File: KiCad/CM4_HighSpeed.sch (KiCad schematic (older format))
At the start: 12 parts, among them J1 Conn_02x02_Odd_Even, J2 Conn_01x22_Female, J3 Conn_01x22_Female, J4 Conn_01x22_Female, J5 Conn_01x22_Female, J6 1888811-1, U5 AP2822CKETR-G1

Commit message: Removing Display0 and Camera0
Eliminates the need for J1, R1 and R2. Also removed.
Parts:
- removed J1: Conn_02x02_Odd_Even, CM4_MATX:PinHeader_2x02_P2.54mm_Vertical, symbol Connector_Generic:Conn_02x02_Odd_Even
- removed J2, J4: Conn_01x22_Female, CM4_MATX:Hirose_FH12-22S-0.5SH_1x22-1MP_P0.50mm_Horizontal, symbol Connector:Conn_01x22_Female
- removed R1, R2: 2.2K 1%, symbol Device:R_Small
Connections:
- net labels removed: GPIO_VREF, ID_SC, ID_SD, SCL1, SDA1
- wire segments 299 -> 241
- no-connect marks 19 -> 8
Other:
- note added: "Camera Connector"
- note added: "Display Connector"
- note removed: "Camera Connectors"
- note removed: "Display Connectors"
- note removed: "Jumpers to be fitted if Camera0 or Display0 are used"
- moved on the sheet: J3, J5

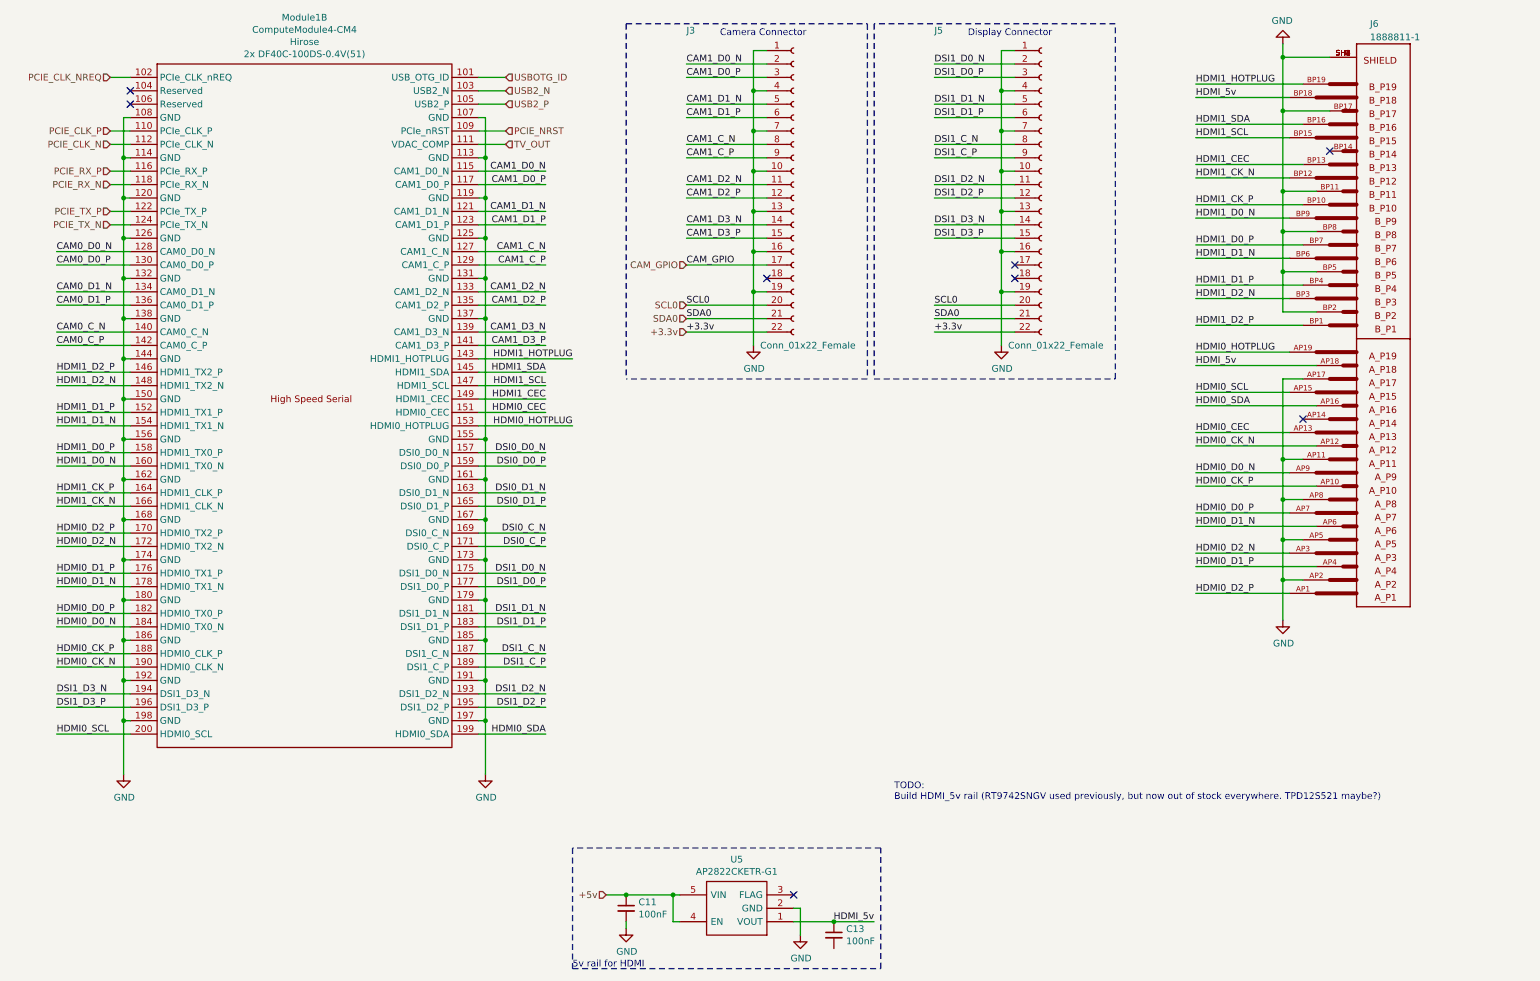
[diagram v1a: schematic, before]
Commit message: PCIe Wiring, resistor value adjustments, and a bunch of small ERC fixes.
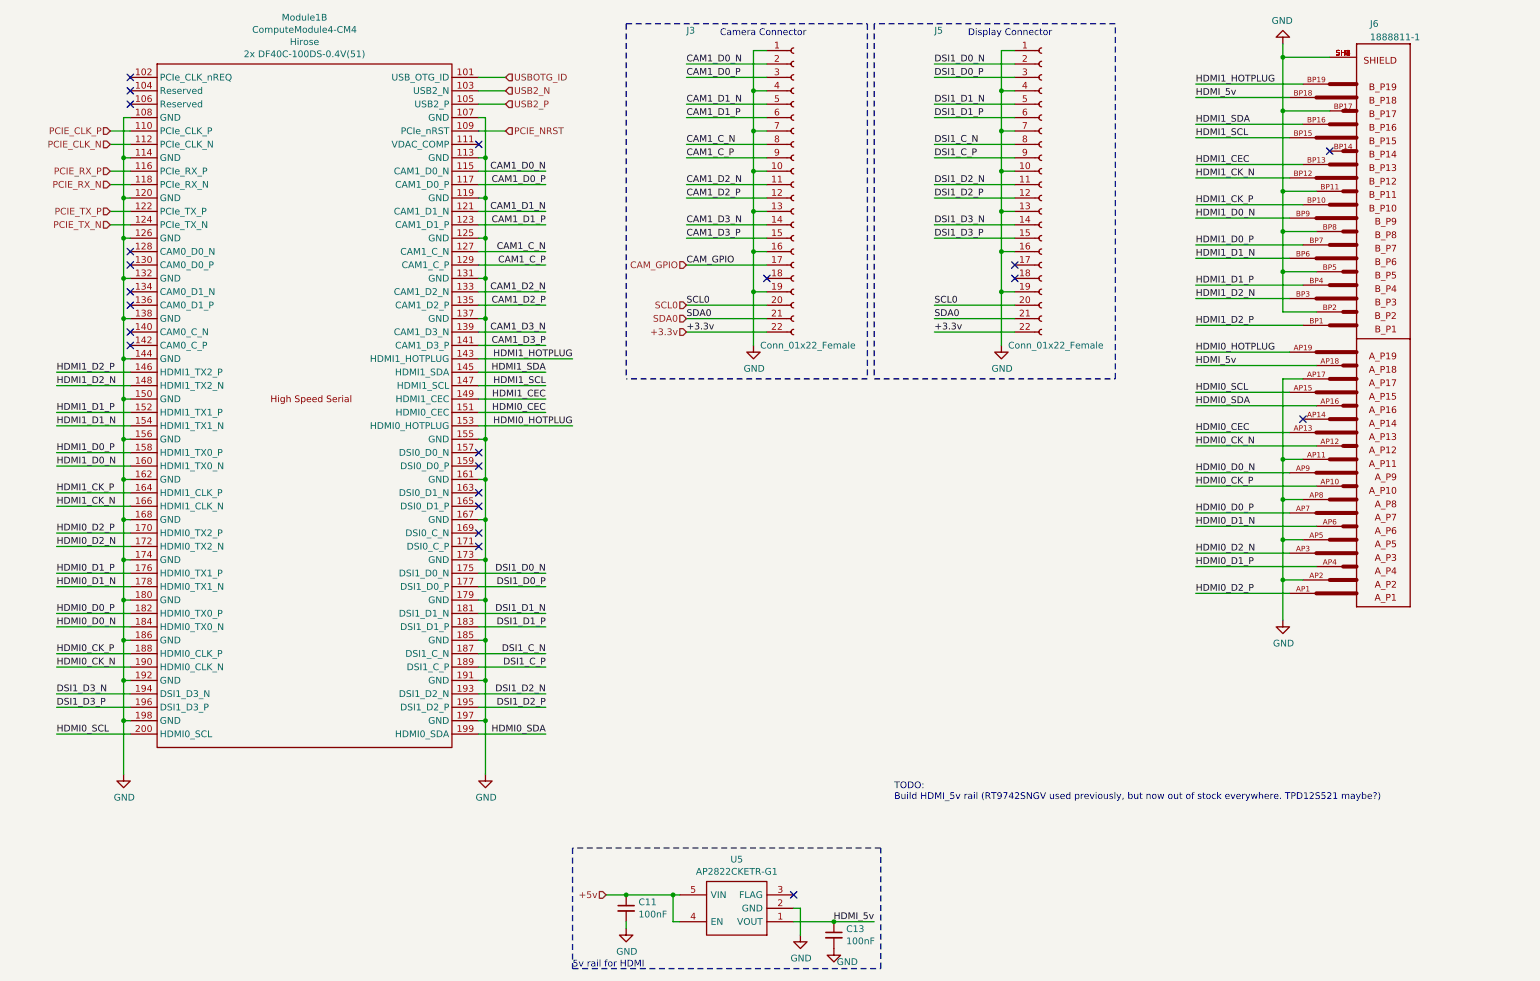
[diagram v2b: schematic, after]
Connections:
- net GND: now also C13.2
- net CAM0_C_N: no longer names the net of Module1.140 (CAM0_C_N)
- net CAM0_C_P: no longer names the net of Module1.142 (CAM0_C_P)
- net CAM0_D0_N: no longer names the net of Module1.128 (CAM0_D0_N)
- net CAM0_D0_P: no longer names the net of Module1.130 (CAM0_D0_P)
- net CAM0_D1_N: no longer names the net of Module1.134 (CAM0_D1_N)
- net CAM0_D1_P: no longer names the net of Module1.136 (CAM0_D1_P)
- net DSI0_C_N: no longer names the net of Module1.169 (DSI0_C_N)
- net DSI0_C_P: no longer names the net of Module1.171 (DSI0_C_P)
- net DSI0_D0_N: no longer names the net of Module1.157 (DSI0_D0_N)
- net DSI0_D0_P: no longer names the net of Module1.159 (DSI0_D0_P)
- net DSI0_D1_N: no longer names the net of Module1.163 (DSI0_D1_N)
- net DSI0_D1_P: no longer names the net of Module1.165 (DSI0_D1_P)
- net PCIE_CLK_NREQ: no longer names the net of Module1.102 (PCIe_CLK_nREQ)
- net TV_OUT: no longer names the net of Module1.111 (VDAC_COMP)
- no-connect marks 8 -> 22
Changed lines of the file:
@@
 Wire Wire Line
 	3950 1700 3950 2000
-Wire Wire Line
-	1150 1100 1300 1100
 $Comp
 L CM4_MATX:ComputeModule4-CM4 Module1
@@
 NoConn ~ 1300 1200
 NoConn ~ 1300 1300
-Text Label 750  2400 0    50   ~ 0
-CAM0_D0_N
-Text Label 750  2500 0    50   ~ 0
-CAM0_D0_P
-Text Label 750  2700 0    50   ~ 0
-CAM0_D1_N
-Text Label 750  2800 0    50   ~ 0
-CAM0_D1_P
-Text Label 750  3000 0    50   ~ 0
-CAM0_C_N
-Text Label 750  3100 0    50   ~ 0
-CAM0_C_P
 Text Label 750  3300 0    50   ~ 0
 HDMI1_D2_P
@@
 Text Label 4400 5400 2    50   ~ 0
 DSI1_C_N
-Text Label 4400 4600 2    50   ~ 0
-DSI0_C_P
-Text Label 4400 4500 2    50   ~ 0
-DSI0_C_N
-Text Label 4400 4300 2    50   ~ 0
-DSI0_D1_P
-Text Label 4400 4200 2    50   ~ 0
-DSI0_D1_N
-Text Label 4400 4000 2    50   ~ 0
-DSI0_D0_P
-Text Label 4400 3900 2    50   ~ 0
-DSI0_D0_N
 Text Label 4400 3600 2    50   ~ 0
 HDMI0_CEC
@@
 Text Label 4400 1800 2    50   ~ 0
 CAM1_D0_N
-Text HLabel 4100 1600 2    50   Input ~ 0
-TV_OUT
 Text HLabel 4100 1500 2    50   Input ~ 0
 PCIE_NRST
@@
 	3900 1500 4100 1500
 Wire Wire Line
-	3900 1600 4100 1600
-Wire Wire Line
 	3900 1800 4400 1800
 Wire Wire Line
@@
 Wire Wire Line
 	4600 3700 3900 3700
-Wire Wire Line
-	4400 3900 3900 3900
-Wire Wire Line
-	3900 4000 4400 4000
-Wire Wire Line
-	4400 4200 3900 4200
-Wire Wire Line
-	3900 4300 4400 4300
-Wire Wire Line
-	4400 4500 3900 4500
-Wire Wire Line
-	3900 4600 4400 4600
 Wire Wire Line
 	4400 4800 3900 4800
@@
 Wire Wire Line
 	750  3300 1300 3300
-Wire Wire Line
-	1300 3100 750  3100
-Wire Wire Line
-	750  3000 1300 3000
-Wire Wire Line
-	1300 2800 750  2800
-Wire Wire Line
-	750  2700 1300 2700
-Wire Wire Line
-	1300 2500 750  2500
-Wire Wire Line
-	1300 2400 750  2400
 Wire Wire Line
 	1300 2200 1150 2200
@@
 Text HLabel 5450 2500 0    50   Input ~ 0
 CAM_GPIO
-Text HLabel 1150 1100 0    50   Input ~ 0
-PCIE_CLK_NREQ
 Text HLabel 1150 1500 0    50   Input ~ 0
 PCIE_CLK_P
@@
 Wire Notes Line
 	8650 700  6850 700
+NoConn ~ 3900 1600
+NoConn ~ 1300 3100
+NoConn ~ 1300 3000
+NoConn ~ 1300 2800
+NoConn ~ 1300 2700
+NoConn ~ 1300 2500
+NoConn ~ 1300 2400
+NoConn ~ 1300 1100
+$Comp
+L power:GND #PWR0232
+U 1 1 6024C813
+P 6550 7600
+F 0 "#PWR0232" H 6550 7350 50  0001 C CNN
+F 1 "GND" H 6650 7500 50  0000 C CNN
+F 2 "" H 6550 7600 50  0001 C CNN
+F 3 "" H 6550 7600 50  0001 C CNN
+	1    6550 7600
+	1    0    0    -1
+$EndComp
+NoConn ~ 3900 4600
+NoConn ~ 3900 4500
+NoConn ~ 3900 4300
+NoConn ~ 3900 4200
+NoConn ~ 3900 4000
+NoConn ~ 3900 3900
 $EndSCHEMATC

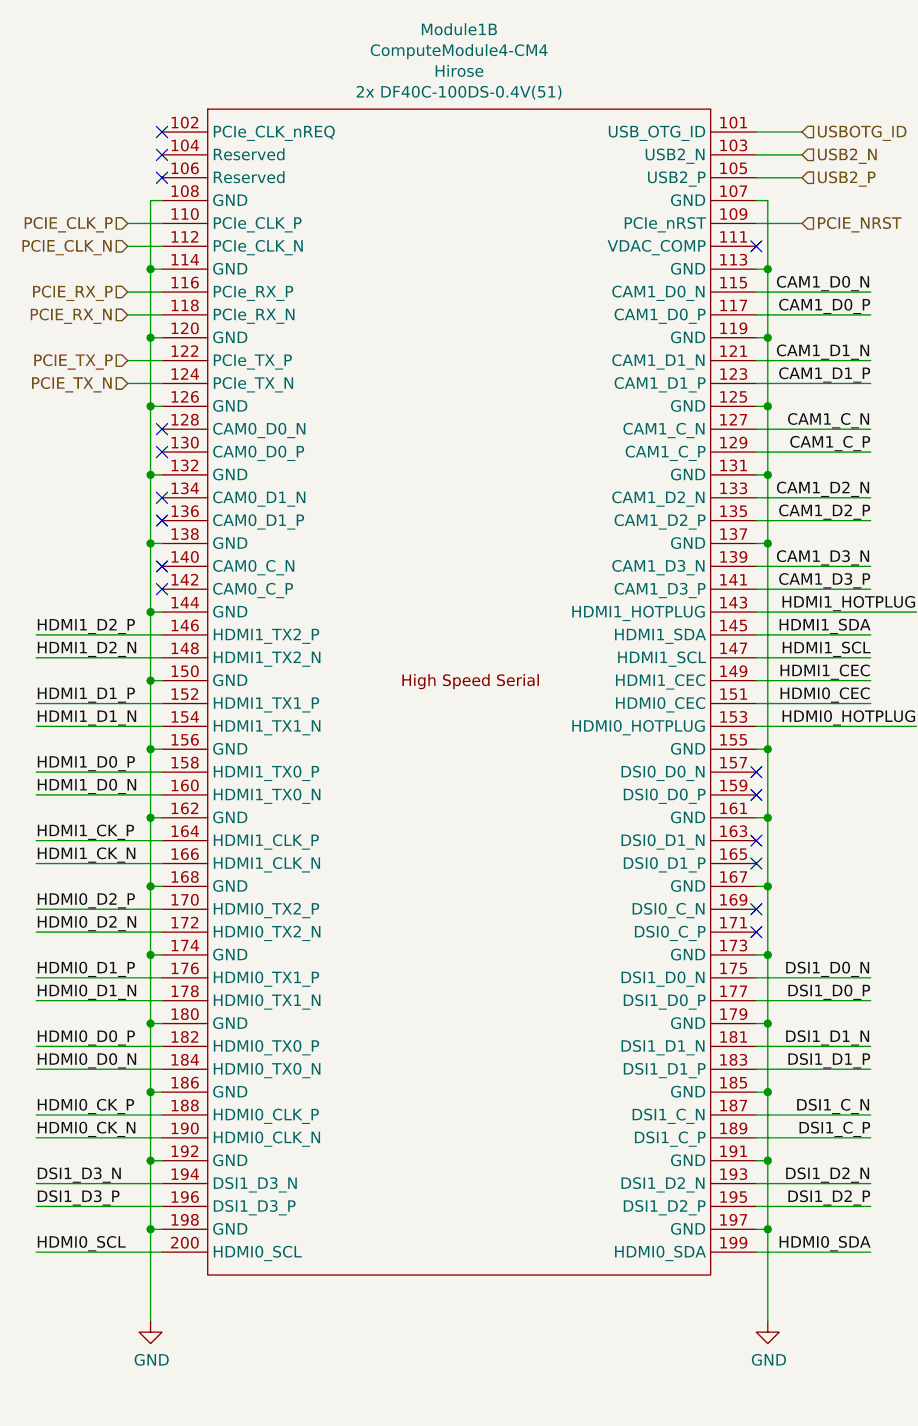
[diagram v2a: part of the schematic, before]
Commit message: Updated CM4 footprints/symbols, mounting holes
This is in a bid to make it more manufactuerable by reducing the need for explanations and questions.
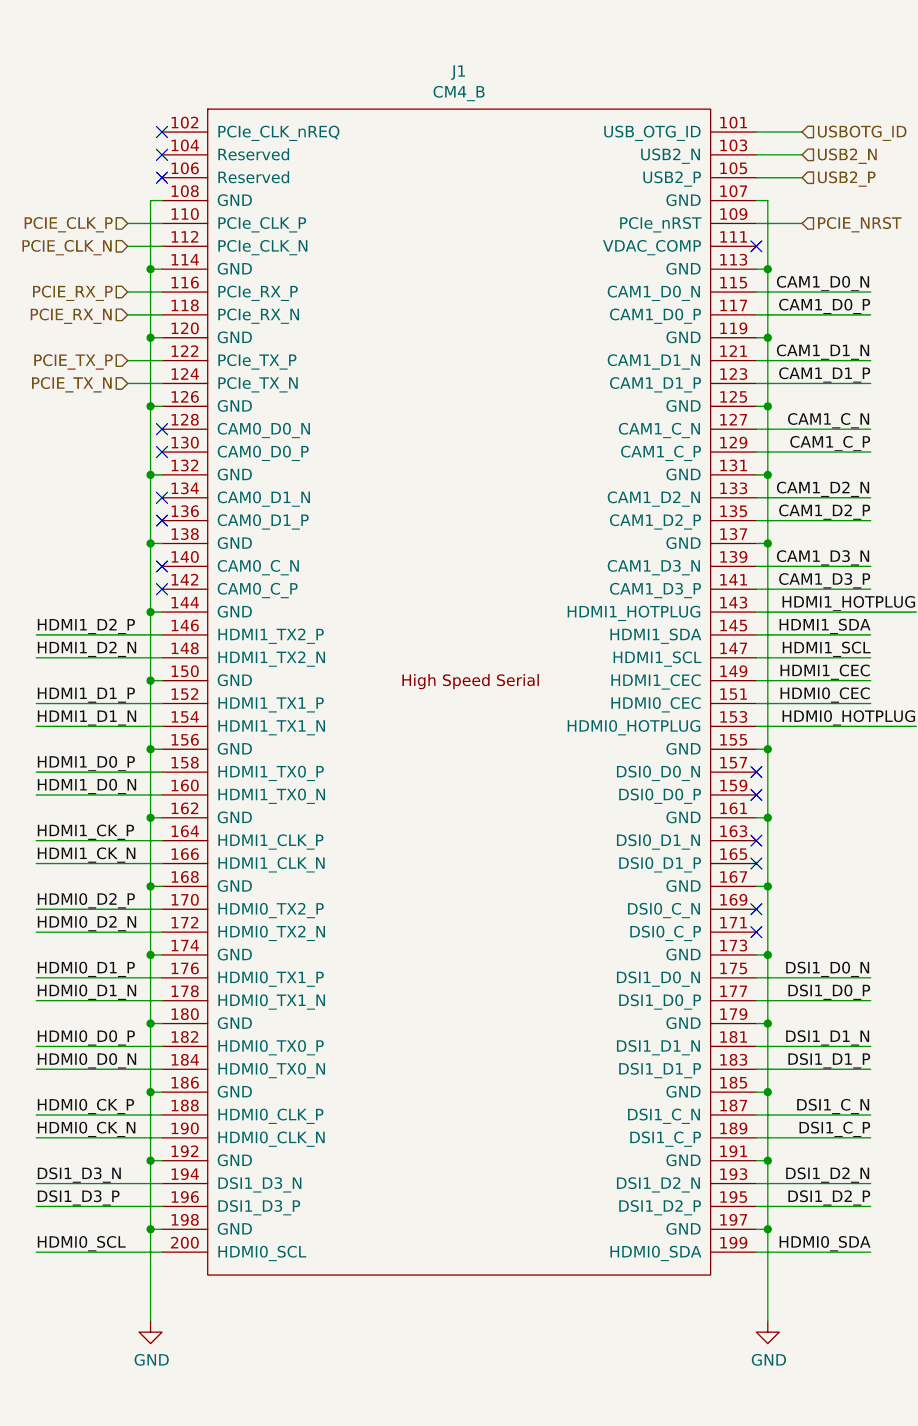
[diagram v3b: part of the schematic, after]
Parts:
- removed Module1: ComputeModule4-CM4, CM4_MATX:rpiCM4, symbol CM4_MATX:ComputeModule4-CM4
- added J1: CM4_B, CM4_MATX:DF40C100DS04V51_B, symbol CM4_MATX:CM4_B
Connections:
- net CAM1_C_N: now also J1.127 (CAM1_C_N)
- net CAM1_C_P: now also J1.129 (CAM1_C_P)
- net CAM1_D0_N: now also J1.115 (CAM1_D0_N)
- net CAM1_D0_P: now also J1.117 (CAM1_D0_P)
- net CAM1_D1_N: now also J1.121 (CAM1_D1_N)
- net CAM1_D1_P: now also J1.123 (CAM1_D1_P)
- net CAM1_D2_N: now also J1.133 (CAM1_D2_N)
- net CAM1_D2_P: now also J1.135 (CAM1_D2_P)
- net CAM1_D3_N: now also J1.139 (CAM1_D3_N)
- net CAM1_D3_P: now also J1.141 (CAM1_D3_P)
- net DSI1_C_N: now also J1.187 (DSI1_C_N)
- net DSI1_C_P: now also J1.189 (DSI1_C_P)
- net DSI1_D0_N: now also J1.175 (DSI1_D0_N)
- net DSI1_D0_P: now also J1.177 (DSI1_D0_P)
- net DSI1_D1_N: now also J1.181 (DSI1_D1_N)
- net DSI1_D1_P: now also J1.183 (DSI1_D1_P)
- net DSI1_D2_N: now also J1.193 (DSI1_D2_N)
- net DSI1_D2_P: now also J1.195 (DSI1_D2_P)
- net DSI1_D3_N: now also J1.194 (DSI1_D3_N)
- net DSI1_D3_P: now also J1.196 (DSI1_D3_P)
- net GND: now also J1.107 (GND), J1.108 (GND), J1.113 (GND), J1.114 (GND), J1.119 (GND), J1.120 (GND), J1.125 (GND), J1.126 (GND), J1.131 (GND), J1.132 (GND), J1.137 (GND), J1.138 (GND), J1.144 (GND), J1.150 (GND), J1.155 (GND), J1.156 (GND), J1.161 (GND), J1.162 (GND), J1.167 (GND), J1.168 (GND), J1.173 (GND), J1.174 (GND), J1.179 (GND), J1.180 (GND), J1.185 (GND), J1.186 (GND), J1.191 (GND), J1.192 (GND), J1.197 (GND), J1.198 (GND)
- net HDMI0_CEC: now also J1.151 (HDMI0_CEC)
- net HDMI0_CK_N: now also J1.190 (HDMI0_CLK_N)
- net HDMI0_CK_P: now also J1.188 (HDMI0_CLK_P)
- net HDMI0_D0_N: now also J1.184 (HDMI0_TX0_N)
- net HDMI0_D0_P: now also J1.182 (HDMI0_TX0_P)
- net HDMI0_D1_N: now also J1.178 (HDMI0_TX1_N)
- net HDMI0_D1_P: now also J1.176 (HDMI0_TX1_P)
- net HDMI0_D2_N: now also J1.172 (HDMI0_TX2_N)
- net HDMI0_D2_P: now also J1.170 (HDMI0_TX2_P)
- net HDMI0_HOTPLUG: now also J1.153 (HDMI0_HOTPLUG)
- net HDMI0_SCL: now also J1.200 (HDMI0_SCL)
- net HDMI0_SDA: now also J1.199 (HDMI0_SDA)
- net HDMI1_CEC: now also J1.149 (HDMI1_CEC)
- net HDMI1_CK_N: now also J1.166 (HDMI1_CLK_N)
- net HDMI1_CK_P: now also J1.164 (HDMI1_CLK_P)
- net HDMI1_D0_N: now also J1.160 (HDMI1_TX0_N)
- net HDMI1_D0_P: now also J1.158 (HDMI1_TX0_P)
- net HDMI1_D1_N: now also J1.154 (HDMI1_TX1_N)
- net HDMI1_D1_P: now also J1.152 (HDMI1_TX1_P)
- net HDMI1_D2_N: now also J1.148 (HDMI1_TX2_N)
- net HDMI1_D2_P: now also J1.146 (HDMI1_TX2_P)
- net HDMI1_HOTPLUG: now also J1.143 (HDMI1_HOTPLUG)
- net HDMI1_SCL: now also J1.147 (HDMI1_SCL)
- net HDMI1_SDA: now also J1.145 (HDMI1_SDA)
- net PCIE_CLK_N: now also J1.112 (PCIe_CLK_N)
- net PCIE_CLK_P: now also J1.110 (PCIe_CLK_P)
- net PCIE_NRST: now also J1.109 (PCIe_nRST)
- net PCIE_RX_N: now also J1.118 (PCIe_RX_N)
- net PCIE_RX_P: now also J1.116 (PCIe_RX_P)
- net PCIE_TX_N: now also J1.124 (PCIe_TX_N)
- net PCIE_TX_P: now also J1.122 (PCIe_TX_P)
- net USB2_N: now also J1.103 (USB2_N)
- net USB2_P: now also J1.105 (USB2_P)
- net USBOTG_ID: now also J1.101 (USB_OTG_ID)
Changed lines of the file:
@@
 Sheet 2 16
 Title "CM4_MATX: CM4 High Speed IO"
-Date "2020-12-28"
+Date "2021-02-08"
 Rev "0.1"
 Comp "Copyright Oliver Møller/@TheGuyDanish 2020, CERN OHL-P v2"
@@
 Wire Wire Line
 	3950 1700 3950 2000
-$Comp
-L CM4_MATX:ComputeModule4-CM4 Module1
-U 2 1 5FB73006
-P 350 950
-AR Path="/5FB73006" Ref="Module1"  Part="2"
-AR Path="/5FB441BA/5FB73006" Ref="Module1"  Part="2"
-F 0 "Module1" H 2600 1247 50  0000 C CNN
-F 1 "ComputeModule4-CM4" H 2600 1156 50  0000 C CNN
-F 2 "CM4_MATX:rpiCM4" H -1250 800 50  0001 C CNN
-F 3 "" H -1250 800 50  0001 C CNN
-F 4 "Hirose" H 2600 1065 50  0000 C CNN "Manufacturer"
-F 5 "2x DF40C-100DS-0.4V(51)" H 2600 974 50  0000 C CNN "Manufacturer Part Number"
-	2    350  950
-	1    0    0    -1
-$EndComp
 NoConn ~ 1300 1200
 NoConn ~ 1300 1300
@@
 NoConn ~ 3900 4000
 NoConn ~ 3900 3900
+$Comp
+L CM4_MATX:CM4_B J1
+U 1 1 60257464
+P 1500 1000
+F 0 "J1" H 2600 1165 50  0000 C CNN
+F 1 "CM4_B" H 2600 1074 50  0000 C CNN
+F 2 "CM4_MATX:DF40C100DS04V51_B" H 2650 1250 50  0001 C CNN
+F 3 "https://datasheets.raspberrypi.org/cm4/cm4-datasheet.pdf" H 1500 1000 50  0001 C CNN
+	1    1500 1000
+	1    0    0    -1
+$EndComp
 $EndSCHEMATC
